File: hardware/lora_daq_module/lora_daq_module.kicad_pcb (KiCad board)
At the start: 4 copper layers, 70 x 40 mm, 75 parts, among them J1 JST3pinfemale, J2 SMA_Edge_50Ω, J3 USB_C_Receptacle_USB2.0_14P, J4 EXT_UART, J5 SWD, J6 Micro_SD_Card_Det1, J7 Conn_01x02, U1 OPA333, U2 ADS1110A0IDBVR, U3 CP2102N-Axx-xQFN20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

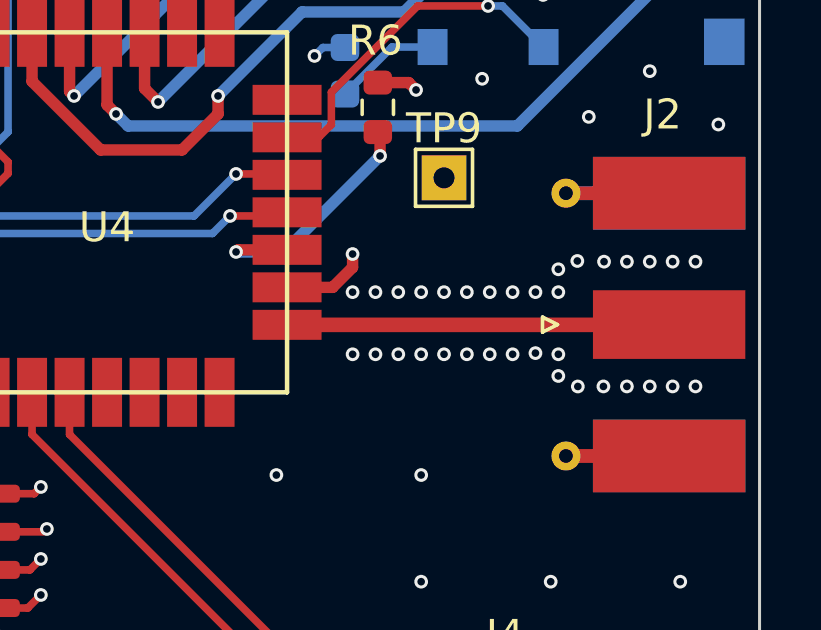
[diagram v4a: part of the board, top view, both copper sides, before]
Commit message: edit board setup for jlcpcb 4 layer 1.6mm 1oz copper in/out and redesign antenna microstrip
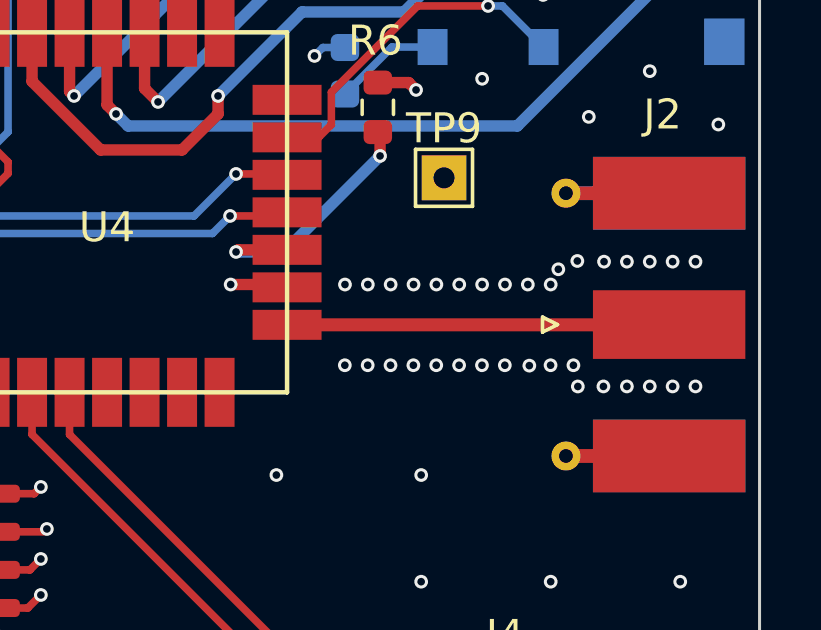
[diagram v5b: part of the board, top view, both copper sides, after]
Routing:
- net GND: track 86.0 -> 85.0 mm
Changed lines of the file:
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@@
 	(generator_version "9.0")
 	(general
-		(thickness 1.7702)
+		(thickness 1.586)
 		(legacy_teardrops no)
 	)
@@
 	)
 	(layers
-		(0 "F.Cu" signal)
+		(0 "F.Cu" signal "Front")
 		(4 "In1.Cu" signal)
 		(6 "In2.Cu" signal)
-		(2 "B.Cu" signal)
+		(2 "B.Cu" signal "Back")
 		(13 "F.Paste" user)
 		(15 "B.Paste" user)
-		(5 "F.SilkS" user "F.Silkscreen")
-		(7 "B.SilkS" user "B.Silkscreen")
+		(5 "F.SilkS" user)
+		(7 "B.SilkS" user)
 		(1 "F.Mask" user)
 		(3 "B.Mask" user)
-		(17 "Dwgs.User" user "User.Drawings")
-		(19 "Cmts.User" user "User.Comments")
 		(25 "Edge.Cuts" user)
 		(27 "Margin" user)
-		(31 "F.CrtYd" user "F.Courtyard")
-		(29 "B.CrtYd" user "B.Courtyard")
+		(31 "F.CrtYd" user)
+		(29 "B.CrtYd" user)
 		(35 "F.Fab" user)
-		(33 "B.Fab" user)
 	)
 	(setup
@@
 			(layer "F.SilkS"
 				(type "Top Silk Screen")
-				(color "White")
-				(material "Liquid Photo")
 			)
 			(layer "F.Paste"
@@
 			(layer "F.Mask"
 				(type "Top Solder Mask")
-				(color "Purple")
-				(thickness 0.0254)
-				(material "Liquid Ink")
-				(epsilon_r 3.3)
-				(loss_tangent 0)
+				(thickness 0.01)
 			)
 			(layer "F.Cu"
 				(type "copper")
-				(thickness 0.0432)
+				(thickness 0.035)
 			)
 			(layer "dielectric 1"
 				(type "prepreg")
-				(thickness 0.2021)
-				(material "FR408-HR")
-				(epsilon_r 3.69)
-				(loss_tangent 0.0091)
+				(color "FR4 natural")
+				(thickness 0.203)
+				(material "FR4")
+				(epsilon_r 4.5)
+				(loss_tangent 0.02)
 			)
 			(layer "In1.Cu"
 				(type "copper")
-				(thickness 0.0175)
+				(thickness 0.03)
 			)
 			(layer "dielectric 2"
 				(type "core")
-				(thickness 1.1938)
-				(material "FR408-HR")
-				(epsilon_r 3.69)
-				(loss_tangent 0.0091)
+				(thickness 1.03)
+				(material "FR4")
+				(epsilon_r 4.5)
+				(loss_tangent 0.02)
 			)
 			(layer "In2.Cu"
 				(type "copper")
-				(thickness 0.0175)
+				(thickness 0.03)
 			)
 			(layer "dielectric 3"
 				(type "prepreg")
-				(thickness 0.2021)
-				(material "FR408-HR")
-				(epsilon_r 3.69)
-				(loss_tangent 0.0091)
+				(thickness 0.203)
+				(material "FR4")
+				(epsilon_r 4.5)
+				(loss_tangent 0.02)
 			)
 			(layer "B.Cu"
 				(type "copper")
-				(thickness 0.0432)
+				(thickness 0.035)
 			)
 			(layer "B.Mask"
 				(type "Bottom Solder Mask")
-				(color "Purple")
-				(thickness 0.0254)
-				(material "Liquid Ink")
-				(epsilon_r 3.3)
-				(loss_tangent 0)
+				(thickness 0.01)
 			)
 			(layer "B.Paste"
@@
 			(layer "B.SilkS"
 				(type "Bottom Silk Screen")
-				(color "White")
-				(material "Liquid Photo")
 			)
-			(copper_finish "ENIG")
+			(copper_finish "None")
 			(dielectric_constraints no)
 		)
 		(pad_to_mask_clearance 0)
+		(solder_mask_min_width 0.1016)
 		(allow_soldermask_bridges_in_footprints no)
 		(tenting front back)
@@
 	)
 	(segment
-		(start 163.42 103.98)
-		(end 161.9 103.98)
-		(width 0.38)
-		(layer "F.Cu")
-		(net 1)
-	)
-	(segment
 		(start 129.74 109.674)
 		(end 129.794 109.728)
@@
 	)
 	(segment
-		(start 164.084 102.87)
-		(end 164.084 103.316)
-		(width 0.38)
-		(layer "F.Cu")
-		(net 1)
-	)
-	(segment
 		(start 130.048 99.011)
 		(end 130.048 100.076)
@@
 	)
 	(segment
+		(start 161.806 103.886)
+		(end 161.9 103.98)
+		(width 0.38)
+		(layer "F.Cu")
+		(net 1)
+	)
+	(segment
 		(start 143.51 90.157)
 		(end 143.51 89.154)
@@
 	)
 	(segment
+		(start 160.02 103.886)
+		(end 161.806 103.886)
+		(width 0.38)
+		(layer "F.Cu")
+		(net 1)
+	)
+	(segment
 		(start 147.348 93.5)
 		(end 147.828 93.98)
@@
 	)
 	(segment
-		(start 164.084 103.316)
-		(end 163.42 103.98)
-		(width 0.38)
-		(layer "F.Cu")
-		(net 1)
-	)
-	(segment
 		(start 130.7 118.1)
 		(end 130.4 118.4)
@@
 	)
 	(via
-		(at 167.894 106.211143)
+		(at 167.634583 106.576779)
 		(size 0.4572)
 		(drill 0.254)
@@
 	)
 	(via
-		(at 170.942 106.934)
+		(at 171.445429 106.576779)
 		(size 0.4572)
 		(drill 0.254)
@@
 	)
 	(via
-		(at 170.18 104.14)
+		(at 169.926 103.886)
 		(size 0.4572)
 		(drill 0.254)
@@
 	)
 	(via
-		(at 167.893154 104.14)
+		(at 167.639154 103.886)
 		(size 0.4572)
 		(drill 0.254)
@@
 	)
 	(via
-		(at 165.608 106.211143)
+		(at 165.348583 106.576779)
 		(size 0.4572)
 		(drill 0.254)
@@
 	)
 	(via
-		(at 164.846846 106.211143)
+		(at 164.587429 106.576779)
 		(size 0.4572)
 		(drill 0.254)
@@
 	)
 	(via
-		(at 169.418 104.14)
+		(at 169.164 103.886)
 		(size 0.4572)
 		(drill 0.254)
@@
 	)
 	(via
-		(at 167.132 106.211143)
+		(at 166.872583 106.576779)
 		(size 0.4572)
 		(drill 0.254)
@@
 	)
 	(via
-		(at 170.942846 106.211143)
+		(at 170.683429 106.576779)
 		(size 0.4572)
 		(drill 0.254)
@@
 	)
 	(via
-		(at 170.942 104.14)
+		(at 170.688 103.886)
 		(size 0.4572)
 		(drill 0.254)
@@
 	)
 	(via
-		(at 164.084 104.14)
+		(at 163.83 103.886)
 		(size 0.4572)
 		(drill 0.254)
@@
 	)
 	(via
-		(at 164.084 102.87)
+		(at 160.02 103.886)
 		(size 0.4572)
 		(drill 0.254)
@@
 	)
 	(via
-		(at 167.131154 104.14)
+		(at 166.877154 103.886)
 		(size 0.4572)
 		(drill 0.254)
@@
 	)
 	(via
-		(at 166.369154 104.14)
+		(at 166.115154 103.886)
 		(size 0.4572)
 		(drill 0.254)
@@
 	)
 	(via
-		(at 166.37 106.211143)
+		(at 166.110583 106.576779)
 		(size 0.4572)
 		(drill 0.254)
@@
 	)
 	(via
-		(at 164.846 104.14)
+		(at 164.592 103.886)
 		(size 0.4572)
 		(drill 0.254)
@@
 	)
 	(via
-		(at 165.607154 104.14)
+		(at 165.353154 103.886)
 		(size 0.4572)
 		(drill 0.254)
@@
 	)
 	(via
-		(at 169.418 106.211143)
+		(at 169.158583 106.576779)
 		(size 0.4572)
 		(drill 0.254)
@@
 	)
 	(via
-		(at 170.18 106.172)
+		(at 169.97567 106.589417)
 		(size 0.4572)
 		(drill 0.254)
@@
 	)
 	(via
-		(at 168.656 106.211143)
+		(at 168.396583 106.576779)
 		(size 0.4572)
 		(drill 0.254)
@@
 	)
 	(via
-		(at 164.084846 106.211143)
+		(at 163.825429 106.576779)
 		(size 0.4572)
 		(drill 0.254)
@@
 	)
 	(via
-		(at 168.656 104.14)
+		(at 168.402 103.886)
 		(size 0.4572)
 		(drill 0.254)
@@
 		(start 161.9 105.23)
 		(end 174.627665 105.23)
-		(width 0.487)
+		(width 0.4362)
 		(layer "F.Cu")
 		(net 4)
@@
 		(polygon
 			(pts
-				(xy 163.068 104.394) (xy 171.958 104.394) (xy 171.958 105.918) (xy 163.068 105.97946)
+				(xy 163.322 104.394) (xy 171.958 104.394) (xy 171.958 106.172) (xy 163.322 106.172)
 			)
 		)

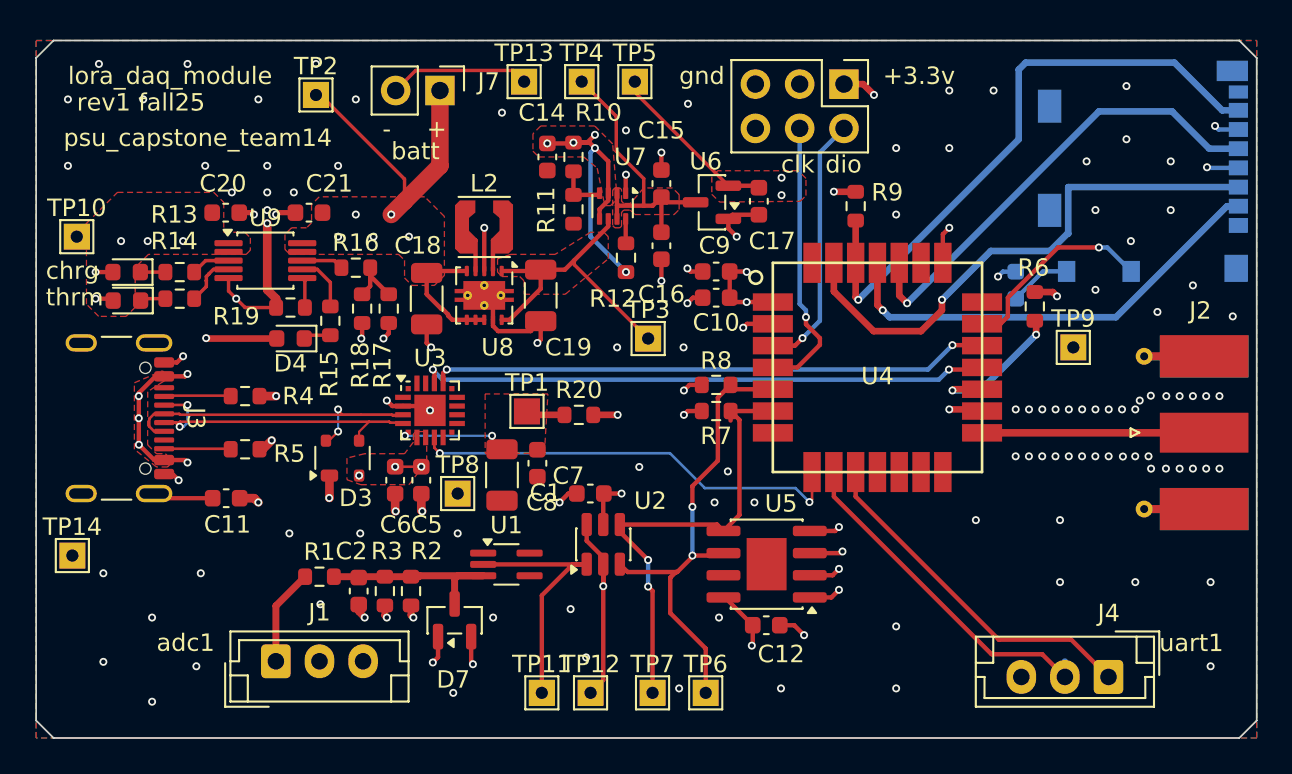
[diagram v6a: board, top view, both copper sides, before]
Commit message: add 0Ω resistors for disabling power circuits, revise adc input buffer and filter based on design review feedback, revise microstrip trace, add hardware reset button, add i2c connector and jst receptacle for battery
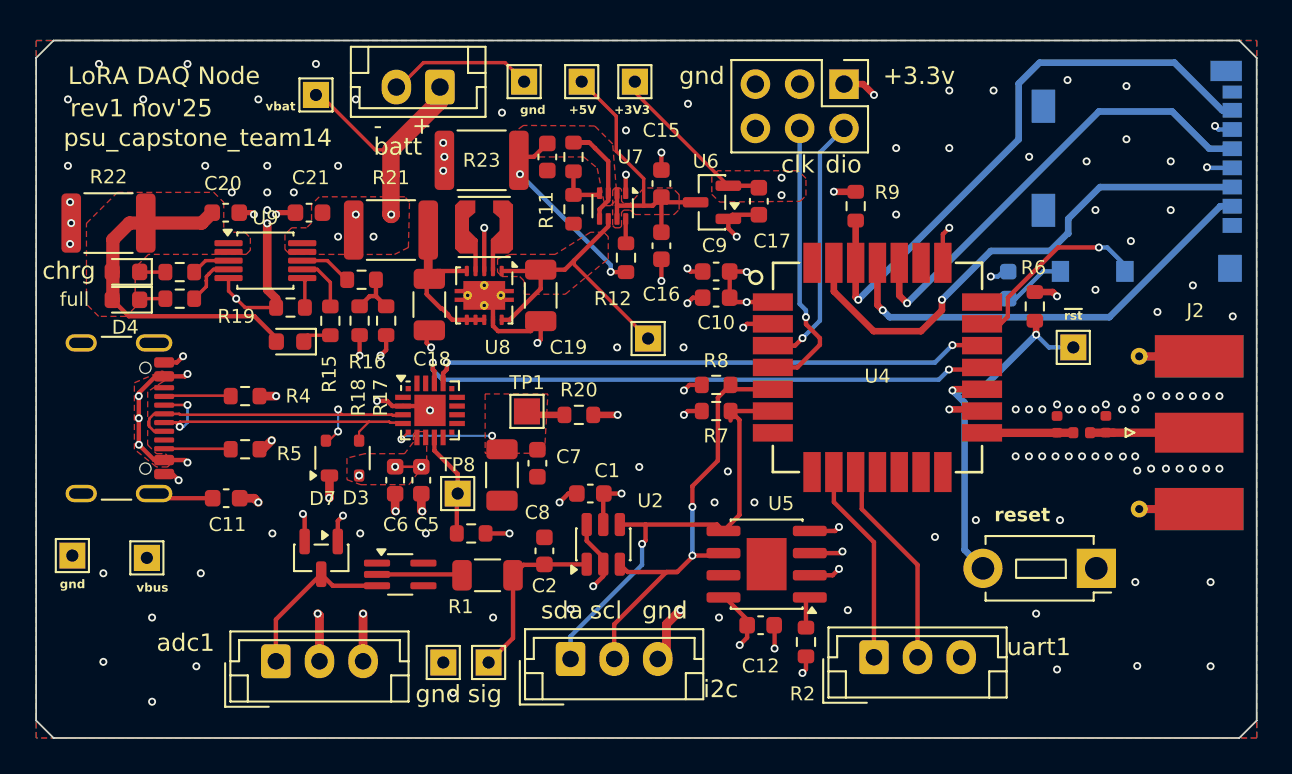
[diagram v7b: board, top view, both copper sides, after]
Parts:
- removed TP11: tp_sig+, TestPoint:TestPoint_THTPad_1.5x1.5mm_Drill0.7mm
- removed TP6: tp_scl, TestPoint:TestPoint_THTPad_1.5x1.5mm_Drill0.7mm
- removed TP7: tp_sda, TestPoint:TestPoint_THTPad_1.5x1.5mm_Drill0.7mm
- added C3: 0, Capacitor_SMD:C_0402_1005Metric, F.Cu at (166.2, 104.7)
- added C4: 0, Capacitor_SMD:C_0402_1005Metric, F.Cu at (169.0, 104.7)
- added J8: EXT_I2C, Connector_JST:JST_EH_B3B-EH-A_1x03_P2.50mm_Vertical, F.Cu at (138.3, 118.2)
- added L1: 0, Inductor_SMD:L_0402_1005Metric, F.Cu at (167.6, 105.2)
- added R21: 0, Resistor_SMD:R_1812_4532Metric, F.Cu at (128.0, 93.6)
- added R22: 0, Resistor_SMD:R_1812_4532Metric, F.Cu at (111.8, 93.2)
- added R23: 0, Resistor_SMD:R_1812_4532Metric, F.Cu at (133.2, 89.6)
- added SW1: MJTP1250, Button_Switch_THT:SW_PUSH_1P1T_6x3.5mm_H5.0_APEM_MJTP1250, F.Cu at (168.4, 113.0)
- added TP15: tp_sig+, TestPoint:TestPoint_THTPad_1.5x1.5mm_Drill0.7mm, F.Cu at (133.6, 118.4)
- C2: value 47n -> 4.7u
- J7: value Conn_01x02 -> jst_b2beh; footprint Connector_PinHeader_2.54mm:PinHeader_1x02_P2.54mm_Vertical -> Connector_JST:JST_EH_B2B-EH-A_1x02_P2.50mm_Vertical
- R1: value 47k -> 47; footprint Resistor_SMD:R_0603_1608Metric -> Resistor_SMD:R_1206_3216Metric
- R2: value 220k -> 4.7k
- R3: value 1k -> 4.7k
- moved R2 22.8 mm to (151.8, 117.2)
- moved TP10 18.9 mm to (114.0, 112.4)
- moved J4 13.5 mm to (155.7, 118.1), turned to 0 degrees
- moved C2 10.9 mm to (136.8, 112.0), turned to 90 degrees
- moved D6 10.2 mm to (122.2, 100.0)
- moved D4 9.70 mm to (112.8, 97.6)
- moved R1 9.64 mm to (133.5, 113.4)
- moved TP12 8.62 mm to (131.0, 118.4)
- moved D7 8.45 mm to (124.0, 112.4), turned to -90 degrees
- moved U1 6.12 mm to (128.5, 113.3)
- moved R3 5.95 mm to (132.6, 111.0), turned to 180 degrees
- moved D5 1.65 mm to (112.8, 96.0)
- moved R16 0.77 mm to (126.3, 96.5)
- moved R17 0.71 mm to (127.7, 98.8)
- moved R18 0.71 mm to (126.2, 98.8)
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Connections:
- C14 pad 1: VBUS -> VBUS_pmux
- C18 pad 1: +VBATT -> Net-(U8-EN)
- C2 pad 1: Net-(U1-+) -> Net-(U2-VIN+)
- C20 pad 1: VBUS -> VBUS_chrg
- D4 pad 2: VBUS -> VBUS_chrg
- D5 pad 2: VBUS -> VBUS_chrg
- D6 pad 2: VBUS -> VBUS_chrg
- D7 pad 3: Net-(U1-+) -> /adc/sig0+
- J1 pad 2: +5VA -> +3.3V
- J4 pad 1: EXT_TX -> EXT_RX
- J4 pad 2: EXT_RX -> EXT_TX
- R1 pad 1: /adc/sig0+ -> Net-(U1--)
- R1 pad 2: Net-(U1-+) -> Net-(U2-VIN+)
- R10 pad 1: VBUS -> VBUS_pmux
- R12 pad 1: VBUS -> VBUS_pmux
- R13 pad 1: Net-(D6-K) -> Net-(D5-K)
- R14 pad 1: Net-(D5-K) -> Net-(D4-K)
- R15 pad 1: Net-(D4-K) -> Net-(D6-K)
- R2 pad 1: Net-(U1-+) -> Net-(U5-A0)
- R2 pad 2: GND -> +3.3V
- R3 pad 1: GND -> +3.3V
- R3 pad 2: Net-(U1-+) -> Net-(U3-~{RST})
- TP8 pad 1: USB_RST -> Net-(U3-~{RST})
- U1 pad 3: Net-(U1-+) -> /adc/sig0+
- U2 pad 1: Net-(U1--) -> Net-(U2-VIN+)
- U3 pad 9: USB_RST -> Net-(U3-~{RST})
- U4 pad 15: Net-(J2-In) -> Net-(U4-RFIO)
- U5 pad 1: GND -> Net-(U5-A0)
- U7 pad 3: VBUS -> VBUS_pmux
- U7 pad 5: VBUS -> VBUS_pmux
- U8 pad 5: +VBATT -> Net-(U8-EN)
- U8 pad 6: +VBATT -> Net-(U8-EN)
- U8 pad 7: +VBATT -> Net-(U8-EN)
- U8 pad 8: +VBATT -> Net-(U8-EN)
- U9 pad 1: VBUS -> VBUS_chrg
- U9 pad 2: VBUS -> VBUS_chrg
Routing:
- net USB_RST: track 25.2 -> 0.00 mm, vias 2 -> 0
- net VBUS: track 33.9 -> 10.9 mm, vias 19 -> 14
- net VBUS_chrg: track 0.00 -> 20.1 mm
- net VBUS_pmux: track 0.00 -> 17.4 mm, vias 0 -> 2
- net Net-(U4-F5/~{RST}): track 8.68 -> 22.0 mm
- net Net-(U1-+): track 11.8 -> 0.00 mm
- net +VBATT: track 24.1 -> 13.9 mm, vias 5 -> 4
- net Net-(U2-VIN+): track 0.00 -> 10.1 mm
- net Net-(U8-EN): track 0.00 -> 10.0 mm
- net Net-(U1--): track 14.8 -> 4.90 mm
- net EXT_TX: track 20.9 -> 12.1 mm
- net EXT_RX: track 19.8 -> 11.6 mm
- net Net-(J2-In): track 13.6 -> 6.55 mm
- net Net-(U3-~{RST}): track 0.00 -> 6.08 mm
- net Net-(U4-RFIO): track 0.00 -> 5.23 mm
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- added copper zone on F.Cu, net VBUS_chrg
- added copper zone on F.Cu, net VBUS_pmux
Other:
- board text added: "+3V3"
- board text added: "+5V"
- board text added: "LoRA DAQ Node"
- board text added: "full"
- board text added: "i2c"
- board text added: "reset"
- board text added: "rev1 nov'25"
- board text added: "scl"
- board text added: "sda"
- board text added: "sig"
- board text added: "vbat"
- board text added: "vbus"
- board text added: "~{rst}"
- board text removed: "lora_daq_module"
- board text removed: "rev1 fall25"
- board text removed: "thrm"
